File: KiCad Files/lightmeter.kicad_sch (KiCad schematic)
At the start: 32 parts, among them J1 LCD Pins, J2 BATTERY, J3 USB_C_5V_POWER, SW1 RESET_SW, SW2 BUTTON2, SW3 BUTTON1, SW4 BUTTON3, SW5 BUTTON4, U1 ATmega328P-A, U2 TP4056, U3 AMS1117-3.3, U4 DW01, U5 FS8205A, Y1 8MHz

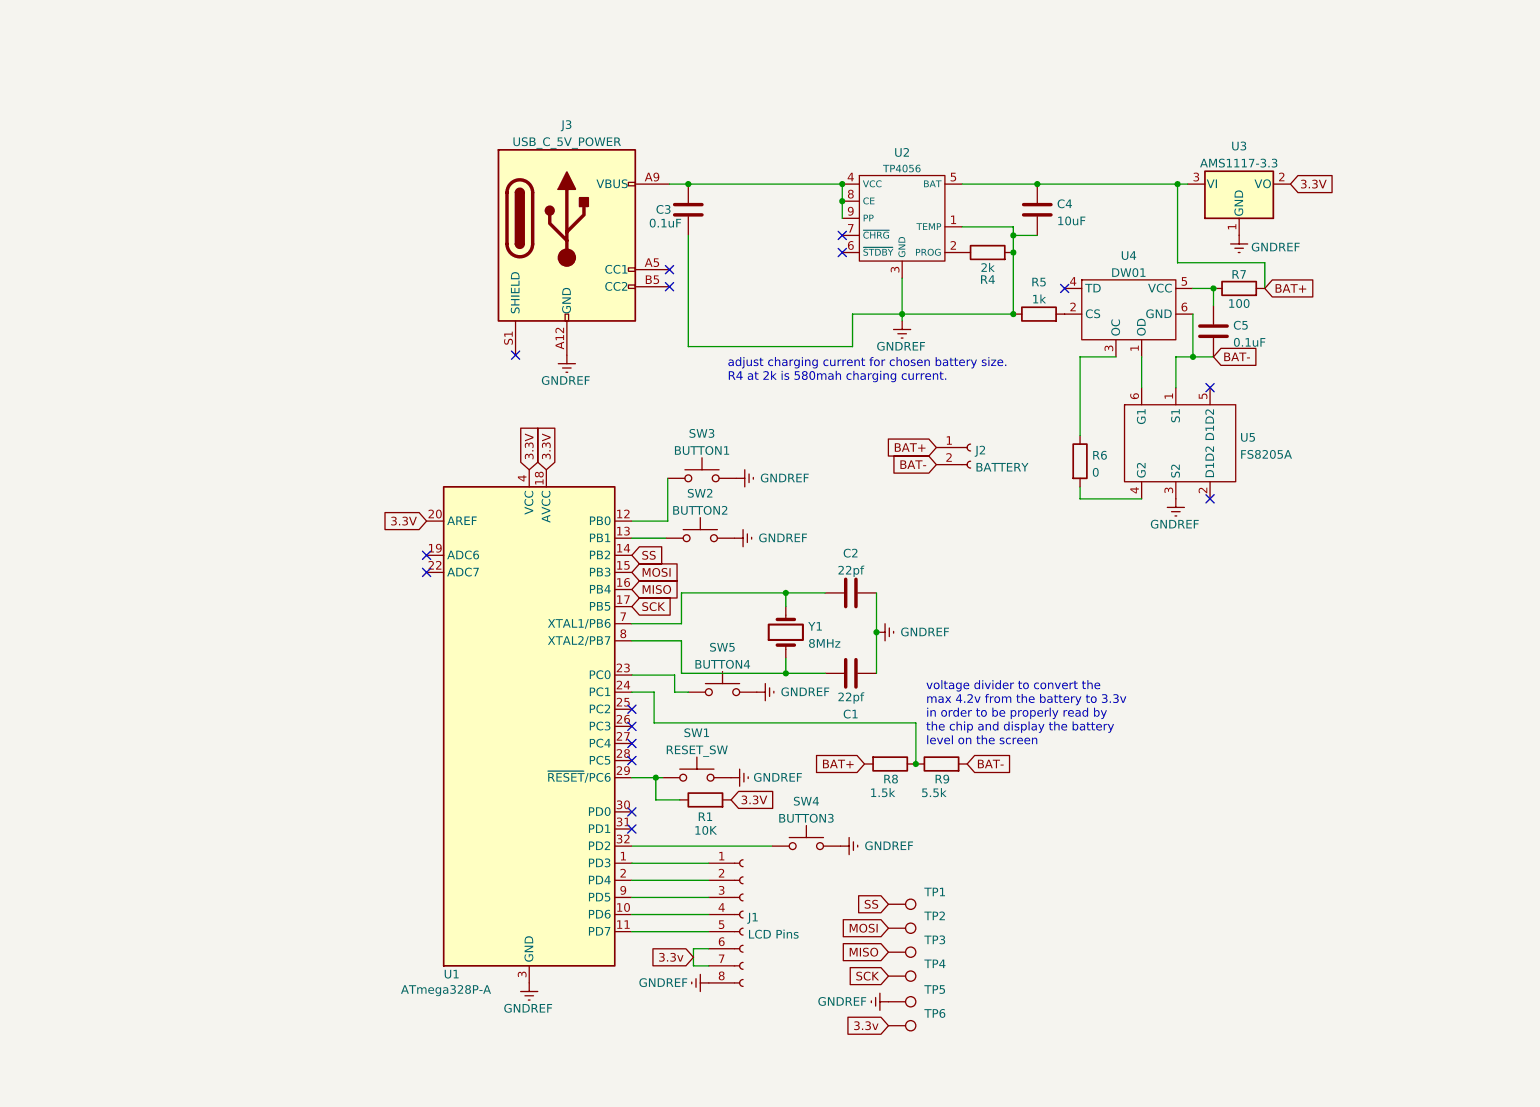
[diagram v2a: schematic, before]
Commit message: Revision 1.2 Schematic
Finally found a library and footprint for the BH1750. I've been calling it the wrong name this entire time huh.
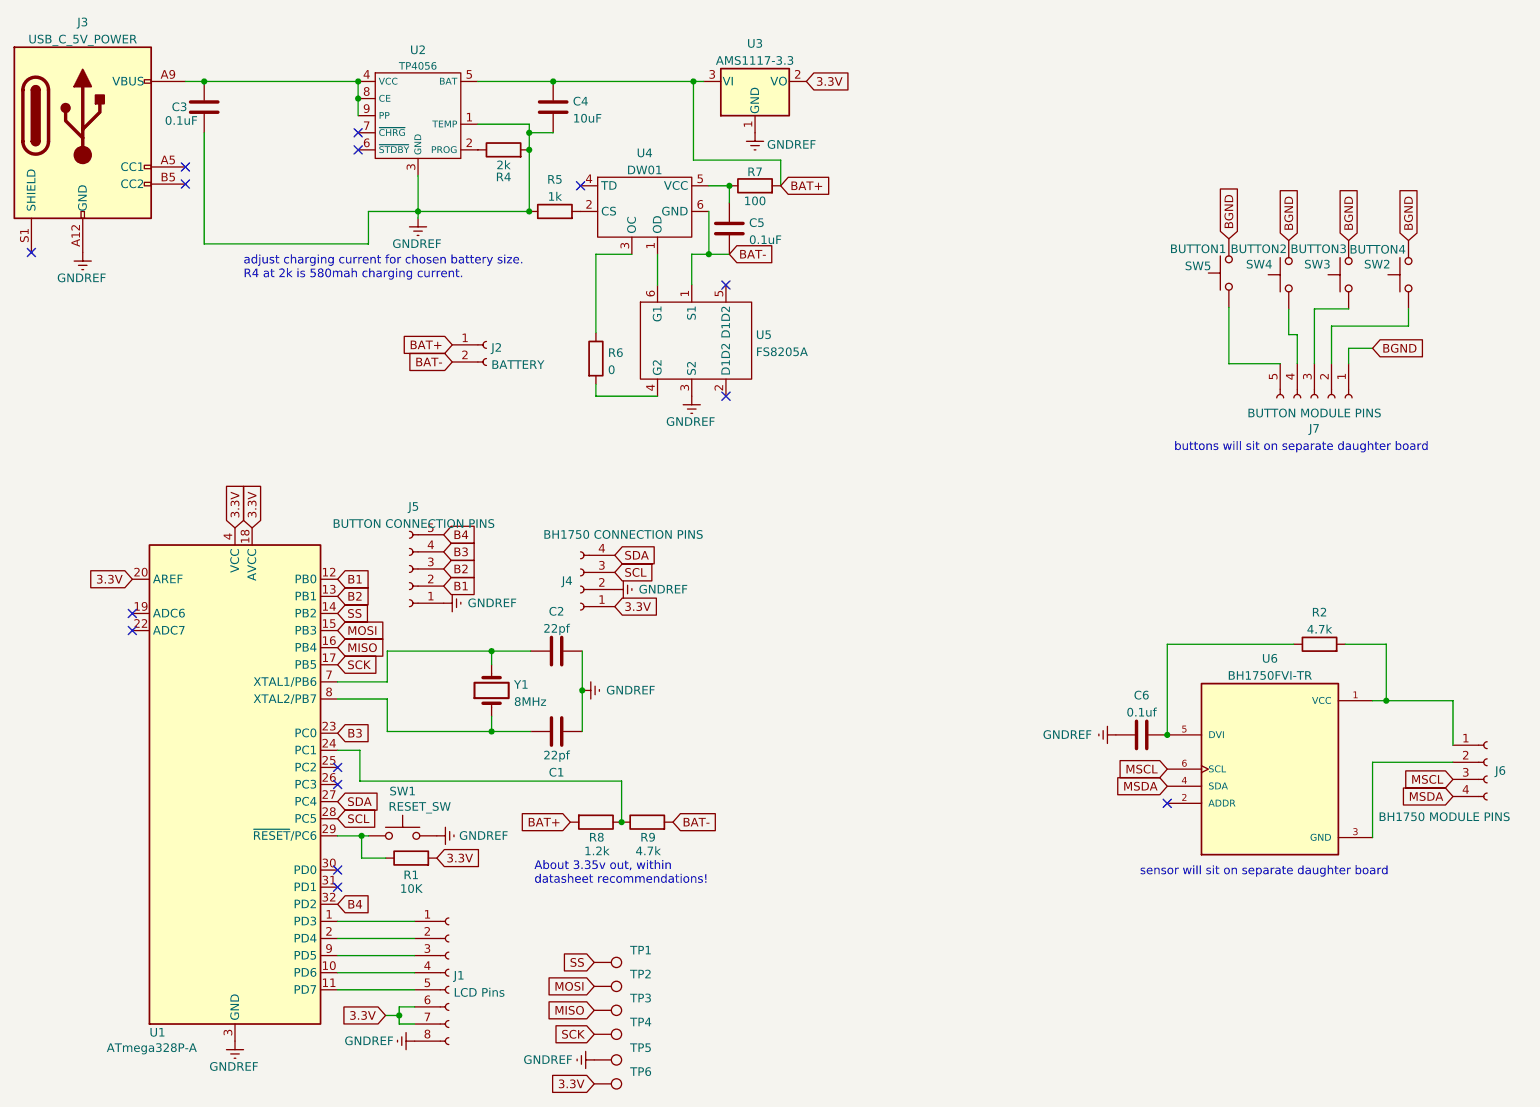
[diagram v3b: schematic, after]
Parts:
- added C6: 0.1uf, Capacitor_SMD:C_0805_2012Metric_Pad1.18x1.45mm_HandSolder, symbol Device:C
- added J4: BH1750 CONNECTION PINS, Connector_PinSocket_2.54mm:PinSocket_1x04_P2.54mm_Vertical, symbol Connector:Conn_01x04_Female
- added J5: BUTTON CONNECTION PINS, Connector_PinSocket_2.54mm:PinSocket_1x05_P2.54mm_Vertical, symbol Connector:Conn_01x05_Female
- added J6: BH1750 MODULE PINS, Connector_PinSocket_2.54mm:PinSocket_1x04_P2.54mm_Vertical, symbol Connector:Conn_01x04_Female
- added J7: BUTTON MODULE PINS, Connector_PinSocket_2.54mm:PinSocket_1x05_P2.54mm_Vertical, symbol Connector:Conn_01x05_Female
- added R2: 4.7k, Resistor_SMD:R_0805_2012Metric_Pad1.20x1.40mm_HandSolder, symbol Device:R
- added U6: BH1750FVI-TR, BH1750FVI-TR:XDCR_BH1750FVI-TR, symbol BH1750FVI-TR:BH1750FVI-TR
- C1, C2, C3, C4, C5: footprint (none) -> Capacitor_SMD:C_0805_2012Metric_Pad1.18x1.45mm_HandSolder
- J1: footprint (none) -> Connector_PinHeader_2.54mm:PinHeader_1x08_P2.54mm_Vertical
- J2: footprint (none) -> Connector_PinSocket_2.54mm:PinSocket_1x02_P2.54mm_Vertical
- J3: footprint (none) -> Connector_USB:USB_C_Receptacle_Palconn_UTC16-G
- R1, R4, R5, R6, R7: footprint (none) -> Resistor_SMD:R_0805_2012Metric_Pad1.20x1.40mm_HandSolder
- R8: value 1.5k -> 1.2k; footprint (none) -> Resistor_SMD:R_0805_2012Metric_Pad1.20x1.40mm_HandSolder
- R9: value 5.5k -> 4.7k; footprint (none) -> Resistor_SMD:R_0805_2012Metric_Pad1.20x1.40mm_HandSolder
- SW1: footprint (none) -> Button_Switch_SMD:SW_SPST_TL3342
- SW2: renamed from SW5; footprint (none) -> Button_Switch_THT:SW_PUSH_6mm
- SW3: renamed from SW4; footprint (none) -> Button_Switch_THT:SW_PUSH_6mm
- SW4: renamed from SW2; footprint (none) -> Button_Switch_THT:SW_PUSH_6mm
- SW5: renamed from SW3; footprint (none) -> Button_Switch_THT:SW_PUSH_6mm
- TP1, TP2, TP3, TP4, TP5, TP6: footprint (none) -> TestPoint:TestPoint_Pad_D2.0mm
- Y1: footprint (none) -> Crystal:Crystal_HC49-U_Vertical
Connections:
- net 3.3v is gone; now on net 3.3V: J1.6 (Pin_6), J1.7 (Pin_7), TP6.1
- net 3.3V: now also J4.1 (Pin_1)
- net GNDREF: now also C6.1, J4.2 (Pin_2), J5.1 (Pin_1); no longer SW2.2, SW3.2, SW4.2, SW5.2
- net at SW4.1: now also J7.4 (Pin_4); no longer U1.13 (PB1)
- net at SW2.1: now also J7.2 (Pin_2); no longer U1.23 (PC0)
- net at SW5.1: now also J7.5 (Pin_5); no longer U1.12 (PB0)
- net SDA: now reaches U1.27 (PC4)
- net SDA: now also J4.4 (Pin_4)
- net SCL: now reaches U1.28 (PC5)
- net SCL: now also J4.3 (Pin_3)
- net at SW3.1: now also J7.3 (Pin_3); no longer U1.32 (PD2)
- new net: J6.1 (Pin_1), R2.2, U6.1 (VCC)
- new net: J6.2 (Pin_2), U6.3 (GND)
- new net: C6.2, R2.1, U6.5 (DVI)
- new net B1: J5.2 (Pin_2), U1.12 (PB0)
- new net B2: J5.3 (Pin_3), U1.13 (PB1)
- new net B3: J5.4 (Pin_4), U1.23 (PC0)
- new net B4: J5.5 (Pin_5), U1.32 (PD2)
- new net BGND: J7.1 (Pin_1), SW2.2, SW3.2, SW4.2, SW5.2
- new net MSCL: J6.3 (Pin_3), U6.6 (SCL)
- new net MSDA: J6.4 (Pin_4), U6.4 (SDA)
- no-connect marks 16 -> 15
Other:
- note added: "About 3.35v out, within datasheet recommendations!"
- note added: "buttons will sit on separate daughter board"
- note added: "sensor will sit on separate daughter board"
- note removed: "voltage divider to convert the max 4.2v from the battery to 3.3v in order to be properly read by the chip and display the battery level on the screen"
- moved on the sheet: C1, C2, C3, C4, C5, J1, J2, J3, R1, R4, R5, R6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
